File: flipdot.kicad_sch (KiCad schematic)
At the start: 47 parts, among them J1 Conn_01x06_Pin, J2 Conn_01x06_Pin, J3 Conn_01x02_Pin, J4 Conn_01x02_Pin, J5 Conn_01x02_Pin, U1 74HC595

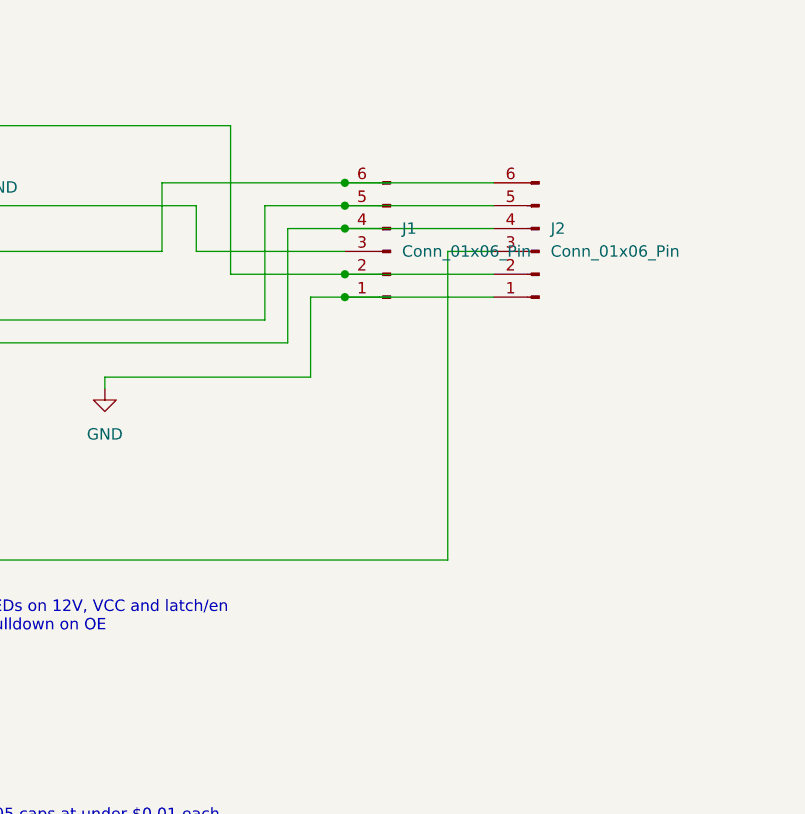
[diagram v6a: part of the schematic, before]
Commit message: use single component for connector
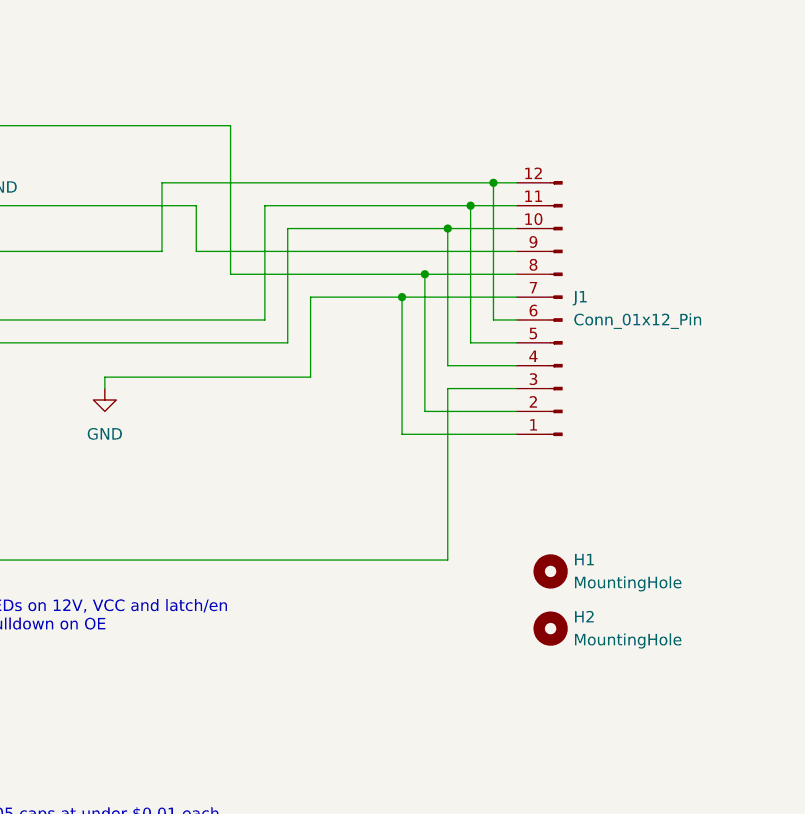
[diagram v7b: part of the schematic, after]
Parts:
- removed J1, J2: Conn_01x06_Pin, Connector_JST:JST_ZH_B6B-ZR_1x06_P1.50mm_Vertical, symbol Connector:Conn_01x06_Pin
- added H1, H2: MountingHole, symbol Mechanical:MountingHole
- added J1: Conn_01x12_Pin, symbol Connector:Conn_01x12_Pin
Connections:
- net CLK: now also J1.12 (Pin_12), J1.6 (Pin_6)
- net DATA_IN: now also J1.9 (Pin_9)
- net DATA_OUT: now also J1.3 (Pin_3)
- net GND: now also J1.1 (Pin_1), J1.7 (Pin_7)
- net LATCH: now also J1.11 (Pin_11), J1.5 (Pin_5)
- net OE*: now also J1.10 (Pin_10), J1.4 (Pin_4)
- net VCC: now also J1.2 (Pin_2), J1.8 (Pin_8)

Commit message: geographic reannotate
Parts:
- H1, H2: footprint (none) -> MountingHole:MountingHole_3.2mm_M3_DIN965
- J4: renamed from J1; footprint (none) -> Connector_JST:JST_ZH_B6B-ZR_1x06_P1.50mm_Vertical
- renumbered C2 to C1, C6 to C10, C4 to C11, C17 to C12, C18 to C13, C19 to C14, C20 to C15, C21 to C16, C22 to C17, C23 to C18, C24 to C19, C1 to C2, C10 to C20, C12 to C21, C15 to C22, C7 to C23, C16 to C24, C8 to C25, C13 to C3, C5 to C4, C14 to C5, C3 to C6, C25 to C7, C9 to C8, C11 to C9, J3 to J1, J5 to J2, J4 to J3, U2 to U1, U3 to U2, U4 to U3, U5 to U4, U1 to U5
